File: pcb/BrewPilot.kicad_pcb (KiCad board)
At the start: 2 copper layers, 170.5 x 116 mm, 31 parts, among them J1 5V Power, J10 Boiler Probe, J11 SOL_L_FUSE, J12 5V_FUSE, J2 Flow Meter Group One, J3 Flow Meter Group Two, J4 FlexGPIO_1, J5 FlexGPIO_2, J6 RelayOut_1, J7 RelayOut2, J8 Solenoid Power, J9 Pump Power, K1 G3MB-202P DC5, K2 G3MB-202P DC5, K3 G3MB-202P DC5, K4 G3MB-202P DC5, K5 G3MB-202P DC5, Q1 BC547, Q2 BC547, Q3 BC547, Q4 BC547, Q5 BC547, U1 esp32

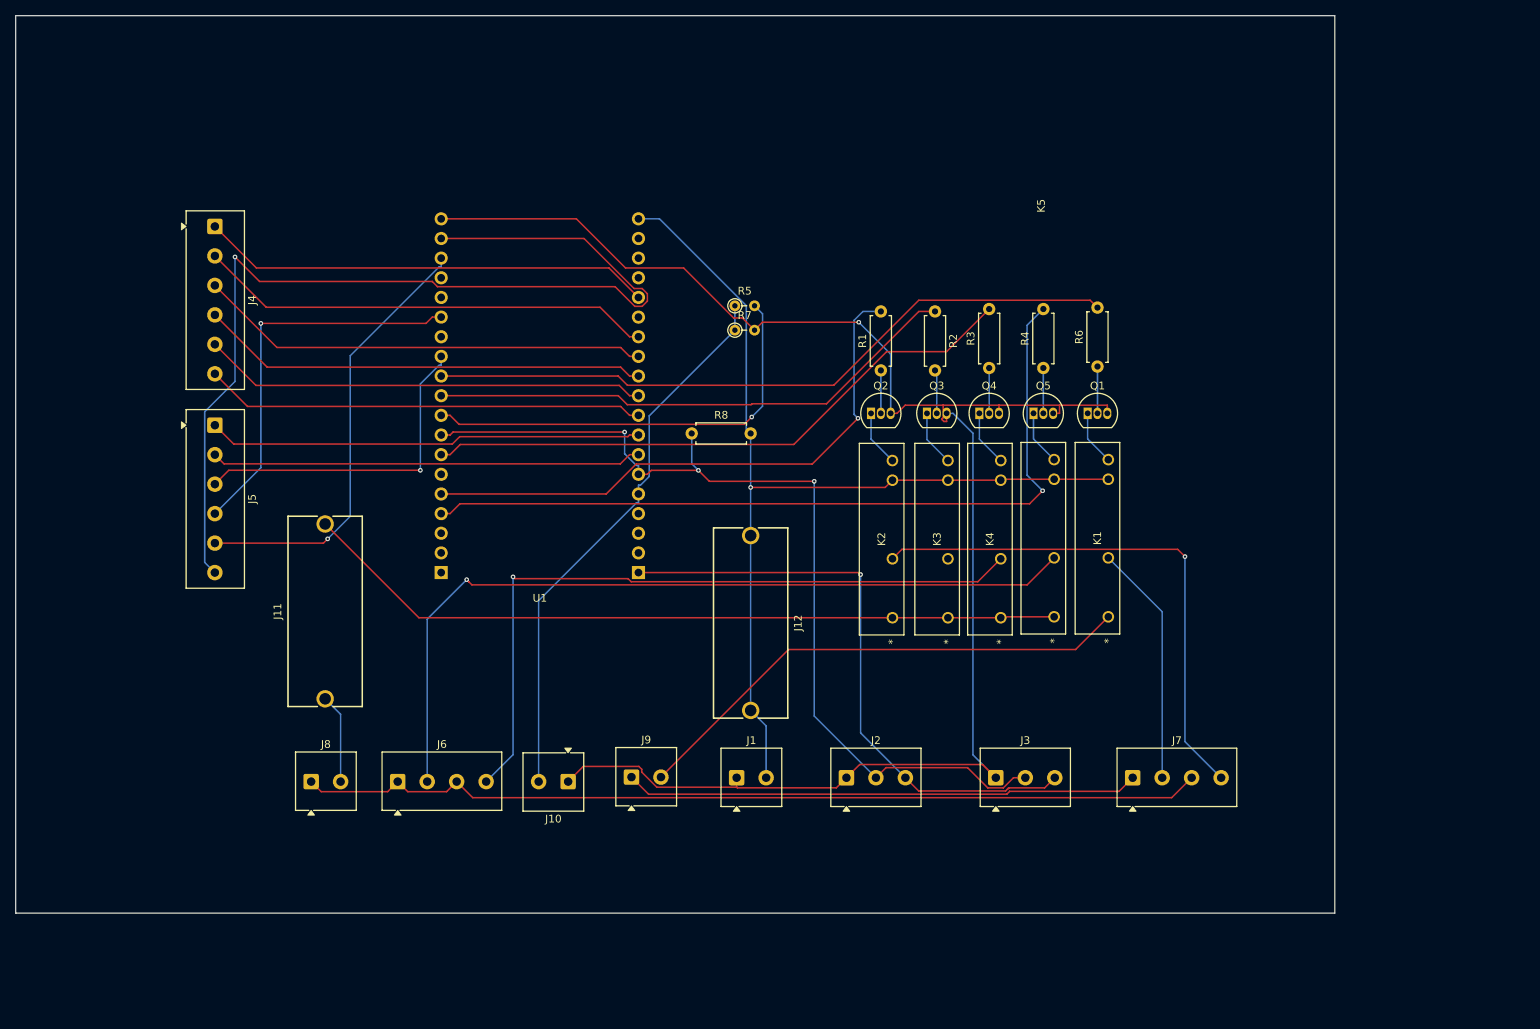
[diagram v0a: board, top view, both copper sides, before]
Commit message: implemented more fixes and initial clean routing pass of the pcb
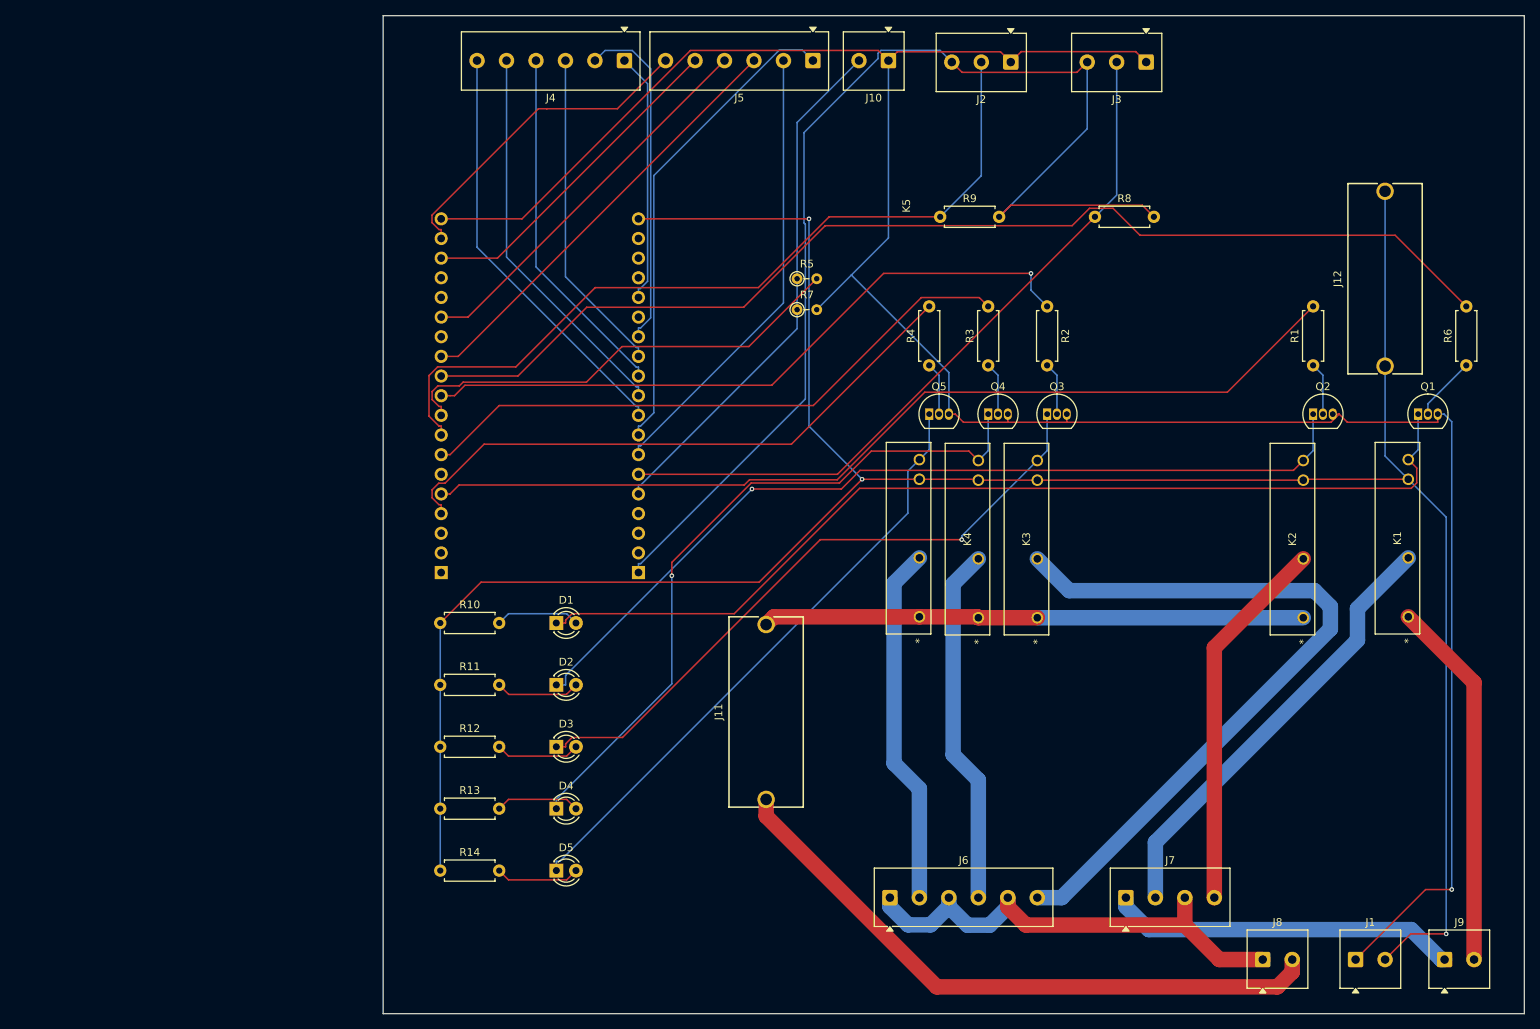
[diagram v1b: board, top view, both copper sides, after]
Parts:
- added D1: PUMP_ON, LED_THT:LED_D3.0mm, F.Cu at (104.9, 114.5)
- added D2: BOILER_FILL_ON, LED_THT:LED_D3.0mm, F.Cu at (104.9, 122.5)
- added D3: GROUP1_ON, LED_THT:LED_D3.0mm, F.Cu at (104.9, 130.5)
- added D4: GROUP2_ON, LED_THT:LED_D3.0mm, F.Cu at (104.9, 138.5)
- added D5: TEA_ON, LED_THT:LED_D3.0mm, F.Cu at (104.9, 146.5)
- added R10: 1k, Resistor_THT:R_Axial_DIN0207_L6.3mm_D2.5mm_P7.62mm_Horizontal, F.Cu at (89.9, 114.5)
- added R11: 1k, Resistor_THT:R_Axial_DIN0207_L6.3mm_D2.5mm_P7.62mm_Horizontal, F.Cu at (89.9, 122.5)
- added R12: 1k, Resistor_THT:R_Axial_DIN0207_L6.3mm_D2.5mm_P7.62mm_Horizontal, F.Cu at (89.9, 130.5)
- added R13: 1k, Resistor_THT:R_Axial_DIN0207_L6.3mm_D2.5mm_P7.62mm_Horizontal, F.Cu at (89.9, 138.5)
- added R14: 1k, Resistor_THT:R_Axial_DIN0207_L6.3mm_D2.5mm_P7.62mm_Horizontal, F.Cu at (89.9, 146.5)
- added R9: 10k, Resistor_THT:R_Axial_DIN0207_L6.3mm_D2.5mm_P7.62mm_Horizontal, F.Cu at (154.5, 62.0)
- J6: footprint TerminalBlock_Phoenix:TerminalBlock_Phoenix_MKDS-1-4-3.81_1x04_P3.81mm_Horizontal -> TerminalBlock_Phoenix:TerminalBlock_Phoenix_MKDS-1-6-3.81_1x06_P3.81mm_Horizontal
- R1, R2, R3, R4, R6: value R -> 4.7k
- R8: value R -> 10k
- moved J8 125.1 mm to (196.2, 158.0)
- moved J9 107.7 mm to (219.7, 158.0)
- moved J10 102.0 mm to (147.8, 41.8)
- moved J2 94.9 mm to (163.6, 42.0), turned to 180 degrees
- moved J3 94.5 mm to (181.1, 42.0), turned to 180 degrees
- moved J12 93.3 mm to (212.0, 70.0), turned to 90 degrees
- moved J5 90.5 mm to (138.1, 41.8), turned to 180 degrees
- moved J1 83.4 mm to (208.2, 158.0)
- moved J6 65.4 mm to (148.0, 150.0)
- moved R8 59.2 mm to (174.5, 62.0)
- moved J11 58.5 mm to (132.0, 126.0)
- moved Q2 57.1 mm to (202.7, 87.5)
- moved J4 57.1 mm to (113.7, 41.8), turned to 180 degrees
- moved R1 55.9 mm to (202.7, 81.2)
- moved K2 53.1 mm to (201.4, 113.8)
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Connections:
- net /SOL_L renamed SOL_L
- J3 pad 2: IN_FLOWMETER_GROUP_ONE -> IN_FLOWMETER_GROUP_TWO
- R8 pad 1: IN_FLOWMETER_GROUP_ONE -> IN_FLOWMETER_GROUP_TWO
- R8 pad 2: 5V -> 3.3V
- U1 pad 6: IN_FLOWMETER_GROUP_ONE -> IN_FLOWMETER_GROUP_TWO
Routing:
- net 5V: track 127.3 -> 332.0 mm, vias 1 -> 3
- net Net-(Q1-C): track 7.09 -> 128.8 mm
- net Net-(Q2-C): track 7.25 -> 115.8 mm, vias 0 -> 1
- net AC_SOLENOID_GROUP_ONE: track 0.00 -> 95.6 mm
- net IN_FLOWMETER_GROUP_TWO: track 0.00 -> 93.9 mm
- net GND: track 220.8 -> 309.4 mm
- net FLEXIBLE_IO_12: track 129.8 -> 42.1 mm, vias 1 -> 0
- net Net-(Q4-C): track 7.25 -> 90.6 mm, vias 0 -> 1
- net Net-(Q3-C): track 7.22 -> 84.5 mm, vias 0 -> 1
- net 3.3V: track 78.4 -> 155.1 mm, vias 1 -> 0
- net Net-(Q5-C): track 7.09 -> 79.2 mm
- net SOL_L: track 11.5 -> 81.7 mm
- net AC_SOLENOID_TEA: track 106.6 -> 46.6 mm, vias 1 -> 0
- net CONTROL_RELAY_PUMP: track 90.3 -> 146.7 mm
- net AC_SOLENOID_NEUTRAL: track 117.9 -> 63.2 mm
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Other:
- board size 170.5 x 116 mm -> 147.5 x 129 mm

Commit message: pcb updates
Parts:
- added C1: 1nF, Capacitor_THT:C_Disc_D5.0mm_W2.5mm_P5.00mm, F.Cu at (159.8, 55.0)
- added C2: 1nF, Capacitor_THT:C_Disc_D5.0mm_W2.5mm_P5.00mm, F.Cu at (177.3, 55.0)
- added C3: 100nF, Capacitor_THT:C_Disc_D5.0mm_W2.5mm_P5.00mm, F.Cu at (144.0, 50.0)
- added D6: PESD3V3, Diode_THT:D_DO-35_SOD27_P7.62mm_Horizontal, F.Cu at (159.8, 51.0)
- added D7: PESD3V3, Diode_THT:D_DO-35_SOD27_P7.62mm_Horizontal, F.Cu at (177.3, 51.0)
- added D8: PESD3V3, Diode_THT:D_DO-35_SOD27_P7.62mm_Horizontal, F.Cu at (136.0, 76.0)
- J12: value 5V_FUSE -> 5V_FUSE_5x20mm; footprint new_local:696108003002 -> Fuse:Fuseholder_Cylinder-5x20mm_Schurter_0031_8201_Horizontal_Open
- moved R7 10.0 mm to (136.0, 84.0)
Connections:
- J1 pad 2: 5V -> 5V_RAW
- J12 pad 1: 5V -> 5V_RAW
- U1 pad 14: unconnected-(U1-GND-Pad14) -> GND
- U1 pad 32: unconnected-(U1-GND-Pad32) -> GND
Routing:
- net 5V_RAW: track 0.00 -> 76.7 mm
- net 5V: track 332.0 -> 280.2 mm, vias 3 -> 2
- net IN_BOILER_PROBE: track 68.0 -> 95.0 mm, vias 0 -> 1
- net GND: track 309.4 -> 298.4 mm, vias 1 -> 2
- net OUT_BOILER_PROBE_VOLTAGE: track 59.5 -> 66.0 mm
- net Net-(Q1-C): vias 0 -> 2
- added copper zone on B.Cu, net GND
- added copper zone on F.Cu, net GND
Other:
- board text added: "5V FUSE"
- board text added: "5V IN"
- board text added: "FILL"
- board text added: "FLEX 1"
- board text added: "FLEX 2"
- board text added: "FLOW 1"
- board text added: "FLOW 2"
- board text added: "G1"
- board text added: "G2"
- board text added: "PROBE"
- board text added: "PUMP"
- board text added: "PUMP PWR"
- board text added: "PUMP/SOL"
- board text added: "SOL FUSE"
- board text added: "SOL OUT"
- board text added: "SOL PWR"
- board text added: "TEA"
